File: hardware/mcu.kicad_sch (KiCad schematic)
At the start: 0 parts

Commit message: RP2350B core sheet: MCU, regulator, crystal, QSPI flash, PSRAM, USB-C, buttons, SWD
- scripts/schlib.py: resolve chained (extends) symbols
- gen_mcu.py: GPIO nets per the architecture map; USB-C data only with Rd

Co-Authored-By: Claude Fable 5.1 <noreply@anthropic.com>
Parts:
- added C20, C21, C22: 4.7u, Capacitor_SMD:C_0805_2012Metric, symbol Device:C
- added C23, C24, C25, C26, C27, C28, C29, C30, C31, C32, C33, C34, C37, C38: 100n, Capacitor_SMD:C_0603_1608Metric, symbol Device:C
- added C35, C36: 15p, Capacitor_SMD:C_0603_1608Metric, symbol Device:C
- added J1: USB-C, Connector_USB:USB_C_Receptacle_HRO_TYPE-C-31-M-12, symbol Connector:USB_C_Receptacle_USB2.0_16P
- added L1: 3.3uH, Inductor_SMD:L_1008_2520Metric, symbol Device:L
- added R20, R23: 1k, Resistor_SMD:R_0603_1608Metric, symbol Device:R
- added R21, R22: 10k, Resistor_SMD:R_0603_1608Metric, symbol Device:R
- added R24, R25: 5k1, Resistor_SMD:R_0603_1608Metric, symbol Device:R
- added R26, R27: 27, Resistor_SMD:R_0603_1608Metric, symbol Device:R
- added SW3: RUN, Button_Switch_SMD:SW_SPST_PTS645Sx43SMTR92, symbol Switch:SW_Push
- added SW4: BOOTSEL, Button_Switch_SMD:SW_SPST_PTS645Sx43SMTR92, symbol Switch:SW_Push
- added TP1: SWCLK, TestPoint:TestPoint_Pad_1.5x1.5mm, symbol Connector:TestPoint
- added TP2: SWDIO, TestPoint:TestPoint_Pad_1.5x1.5mm, symbol Connector:TestPoint
- added TP3: GND, TestPoint:TestPoint_Pad_1.5x1.5mm, symbol Connector:TestPoint
- added U20: RP2350B, Package_DFN_QFN:QFN-80-1EP_10x10mm_P0.4mm_EP3.4x3.4mm, symbol MCU_RaspberryPi:RP2350B
- added U21: W25Q128JVSIQ, Package_SO:SOIC-8_5.3x5.3mm_P1.27mm, symbol Memory_Flash:W25Q128JVS
- added U22: APS6404L-3SQR-SN, Package_SO:SOIC-8_5.3x5.3mm_P1.27mm, symbol Memory_RAM:APS6404L-3SQRx-SN
- added Y1: 12MHz, Crystal:Crystal_SMD_3225-4Pin_3.2x2.5mm, symbol Device:Crystal_GND24
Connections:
- new net: J1.A4 (VBUS), J1.A9 (VBUS), J1.B4 (VBUS), J1.B9 (VBUS)
- new net +3V3: C22.1, C23.1, C24.1, C25.1, C26.1, C27.1, C28.1, C29.1, C30.1, C31.1, C32.1, C33.1, C34.1, C37.1, C38.1, R21.1, R22.1, U20.15 (IOVDD), U20.24 (IOVDD), U20.29 (IOVDD), U20.41 (IOVDD), U20.5 (IOVDD), U20.50 (IOVDD), U20.59 (ADC_AVDD), U20.60 (IOVDD), U20.61 (VREG_AVDD), U20.64 (VREG_VIN), U20.68 (USB_OTP_VDD), U20.69 (QSPI_IOVDD), U20.76 (IOVDD), U21.8 (VCC), U22.8 (VDD)
- new net ASEL: U20.6 (GPIO8)
- new net AUDIO_L: U20.57 (GPIO46/ADC6)
- new net AUDIO_R: U20.38 (GPIO30)
- new net BE_REQ: U20.9 (GPIO11)
- new net BOOTSEL_SW: R23.2, SW4.1
- new net CC1: J1.A5 (CC1), R24.1
- new net CC2: J1.B5 (CC2), R25.1
- new net DVDD: C20.1, C21.1, L1.2, U20.10 (DVDD), U20.32 (DVDD), U20.51 (DVDD), U20.65 (VREG_FB)
- new net GND: C20.2, C21.2, C22.2, C23.2, C24.2, C25.2, C26.2, C27.2, C28.2, C29.2, C30.2, C31.2, C32.2, C33.2, C34.2, C35.2, C36.2, C37.2, C38.2, J1.A1 (GND), J1.A12 (GND), J1.B1 (GND), J1.B12 (GND), J1.SH (SHIELD), R24.2, R25.2, SW3.2, SW4.2, TP3.1, U20.62 (VREG_PGND), U20.81 (GND), U21.4 (GND), U22.4 (VSS), Y1.2 (G), Y1.4 (G)
- new net MD0: U20.77 (GPIO0)
- new net MD1: U20.78 (GPIO1)
- new net MD2: U20.79 (GPIO2)
- new net MD3: U20.80 (GPIO3)
- new net MD4: U20.1 (GPIO4)
- new net MD5: U20.2 (GPIO5)
- new net MD6: U20.3 (GPIO6)
- new net MD7: U20.4 (GPIO7)
- new net OLED_CS: U20.52 (GPIO41/ADC1)
- new net OLED_DC: U20.49 (GPIO40/ADC0)
- new net OLED_MOSI: U20.54 (GPIO43/ADC3)
- new net OLED_SCK: U20.53 (GPIO42/ADC2)
- new net PSRAM_CS: U20.58 (GPIO47/ADC7), U22.1 (~{CE})
- new net QSPI_SCLK: U20.71 (QSPI_SCLK), U21.6 (CLK), U22.6 (SCLK)
- new net QSPI_SD0: U20.72 (QSPI_SD0), U21.5 (DI/IO_{0}), U22.5 (SI/SIO0)
- new net QSPI_SD1: U20.74 (QSPI_SD1), U21.2 (DO/IO_{1}), U22.2 (SO/SIO1)
- new net QSPI_SD2: U20.73 (QSPI_SD2), U21.3 (~{WP}/IO_{2}), U22.3 (SIO2)
- new net QSPI_SD3: U20.70 (QSPI_SD3), U21.7 (~{HOLD}/~{RESET}/IO_{3}), U22.7 (SIO3)
- new net REG_SEL0: U20.25 (GPIO24)
- new net REG_SEL1: U20.26 (GPIO25)
- new net RESET_HOLD: U20.37 (GPIO29)
- new net RUN: R22.2, SW3.1, U20.35 (RUN)
- new net SD_CS: U20.46 (GPIO37)
- new net SD_MISO: U20.45 (GPIO36)
- new net SD_MOSI: U20.48 (GPIO39)
- new net SD_SCK: U20.47 (GPIO38)
- new net SWCLK: TP1.1, U20.33 (SWCLK)
- new net SWDIO: TP2.1, U20.34 (SWDIO)
- new net TAPE_IN: U20.22 (GPIO22)
- new net TAPE_OUT: U20.23 (GPIO23)
- new net USB_DM: R27.2, U20.66 (USB_DM)
- new net USB_DM_C: J1.A7 (D-), J1.B7 (D-), R27.1
- new net USB_DP: R26.2, U20.67 (USB_DP)
- new net USB_DP_C: J1.A6 (D+), J1.B6 (D+), R26.1
- new net VREG_LX: L1.1, U20.63 (VREG_LX)
- new net WAIT_REQ: U20.11 (GPIO12)
- new net WIFI_RX: U20.56 (GPIO45/ADC5)
- new net WIFI_TX: U20.55 (GPIO44/ADC4)
- new net XIN: C35.1, U20.30 (XIN), Y1.1
- new net XOUT: R20.1, U20.31 (XOUT)
- new net XOUT_R: C36.1, R20.2, Y1.3
- new net Z80_A14: U20.12 (GPIO13)
- new net Z80_A15: U20.13 (GPIO14)
- new net nAOE: U20.7 (GPIO9)
- new net nDATA_OE: U20.8 (GPIO10)
- new net nEXROM_L: U20.20 (GPIO20)
- new net nINT_L: U20.21 (GPIO21)
- new net nIORQ_V: U20.16 (GPIO16)
- new net nMRD: U20.28 (GPIO27)
- new net nMREQ_V: U20.14 (GPIO15)
- new net nMWR: U20.36 (GPIO28)
- new net nQSPI_SS: R21.2, R23.1, U20.75 (~{QSPI_SS}), U21.1 (~{CS})
- new net nRD_L: U20.17 (GPIO17)
- new net nREG_STB: U20.27 (GPIO26)
- new net nROSCS_L: U20.19 (GPIO19)
- new net nWR_L: U20.18 (GPIO18)
- no-connect marks 0 -> 11
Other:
- note added: "C23-C34: one per IOVDD, QSPI_IOVDD, USB_OTP_VDD, ADC_AVDD, VREG_AVDD pin, placed at the pin."
- note added: "CS1 = GPIO47 (QMI CS1n). C37/C38 at U21/U22."
- note added: "J1: USB 2.0 only. VBUS and SBU unconnected."
- note added: "L1/C20/C21: RP2350 internal 1.1 V core regulator. C22 at VREG_VIN."
- note added: "R24/R25 5.1 k Rd. R26/R27 27 R series."
- note added: "RP2350B core per the RP2350 hardware design guide. GPIO map: docs/v3-architecture.md section 7. GP31-GP35 spare."
- note added: "TP1-TP3: SWD debug pads."
- note added: "U21 boot flash (XIP CS0). U22 PSRAM on the same QSPI bus,"
- note added: "USB-C is data only: VBUS is not connected to the card. Rd on CC1/CC2 so a Type-C host attaches."
- note added: "Y1: 12 MHz, e.g. ABM8-272-T3 (CL 10 pF). C35/C36 15 pF, R20 1 k in series with XOUT."
- note removed: "RP2350B, W25Q128 QSPI flash, APS6404L PSRAM (CS1=GP47), 12 MHz crystal, USB-C, BOOTSEL/RUN, SWD pads"

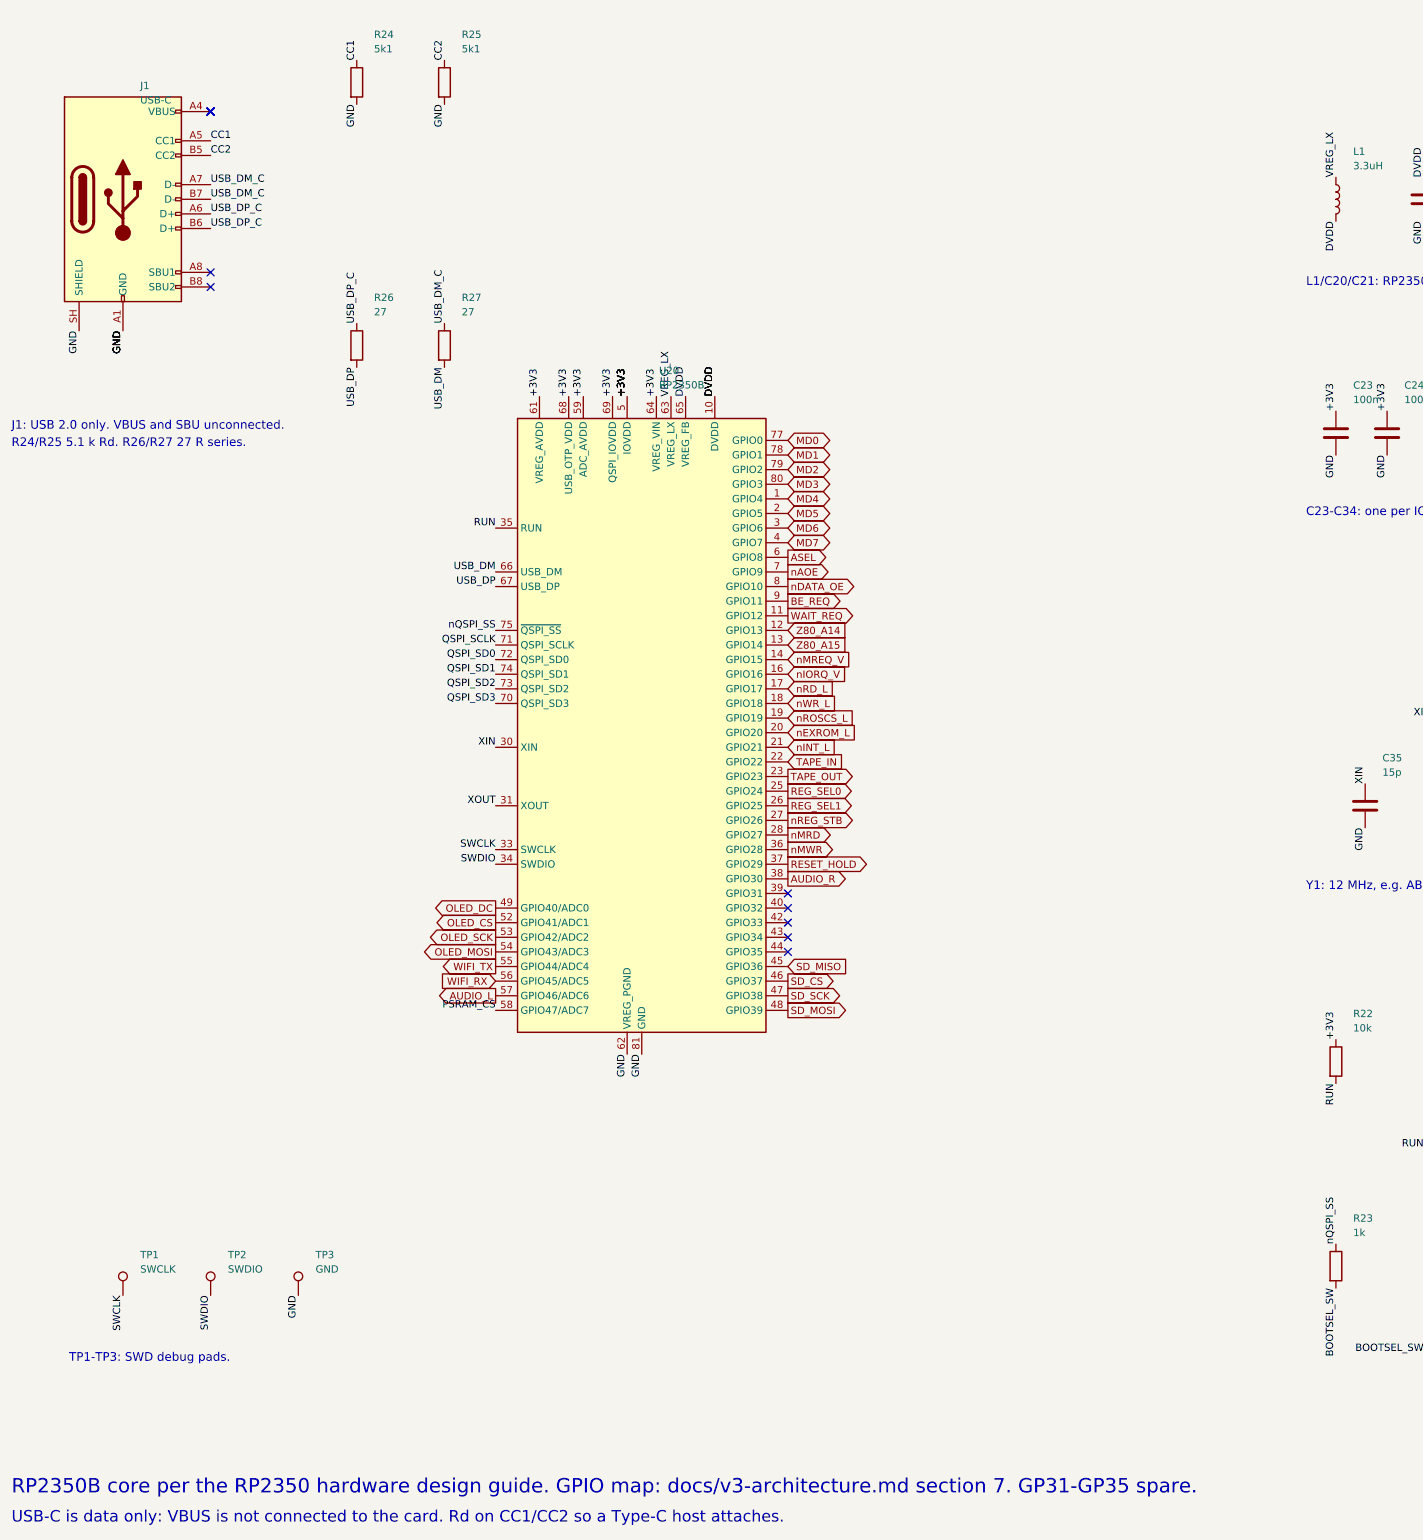
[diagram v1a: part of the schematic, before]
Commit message: Remaining sheets: power, SD and display, WiFi, audio, joystick; ERC clean
- Power: Schottky diode-OR of edge +5V and USB VBUS (card runs from the
  2068/expansion bus, USB alone, or both), two TLV1117LV33 LDOs, bulk caps
- SD: Hirose DM3AT in SPI mode with series R, pull-ups, card detect to STAT
- OLED: 7-pin header (Waveshare 1.27in 128x96 SSD1351) on SPI1
- WiFi: ESP32-C3-WROOM-02 on UART, EN/boot from CTL, IO8 pull-up
- Audio: PWM low-pass, 2068 SOUND mix, MCP6002 buffers, 3.5 mm jack
- Joystick: DE-9 Kempston with pull-ups, series R, optional +5V jumper
- Memory sheet: activity LED on CTL bit 6
- Docs: power decision updated

Co-Authored-By: Claude Fable 5.1 <noreply@anthropic.com>
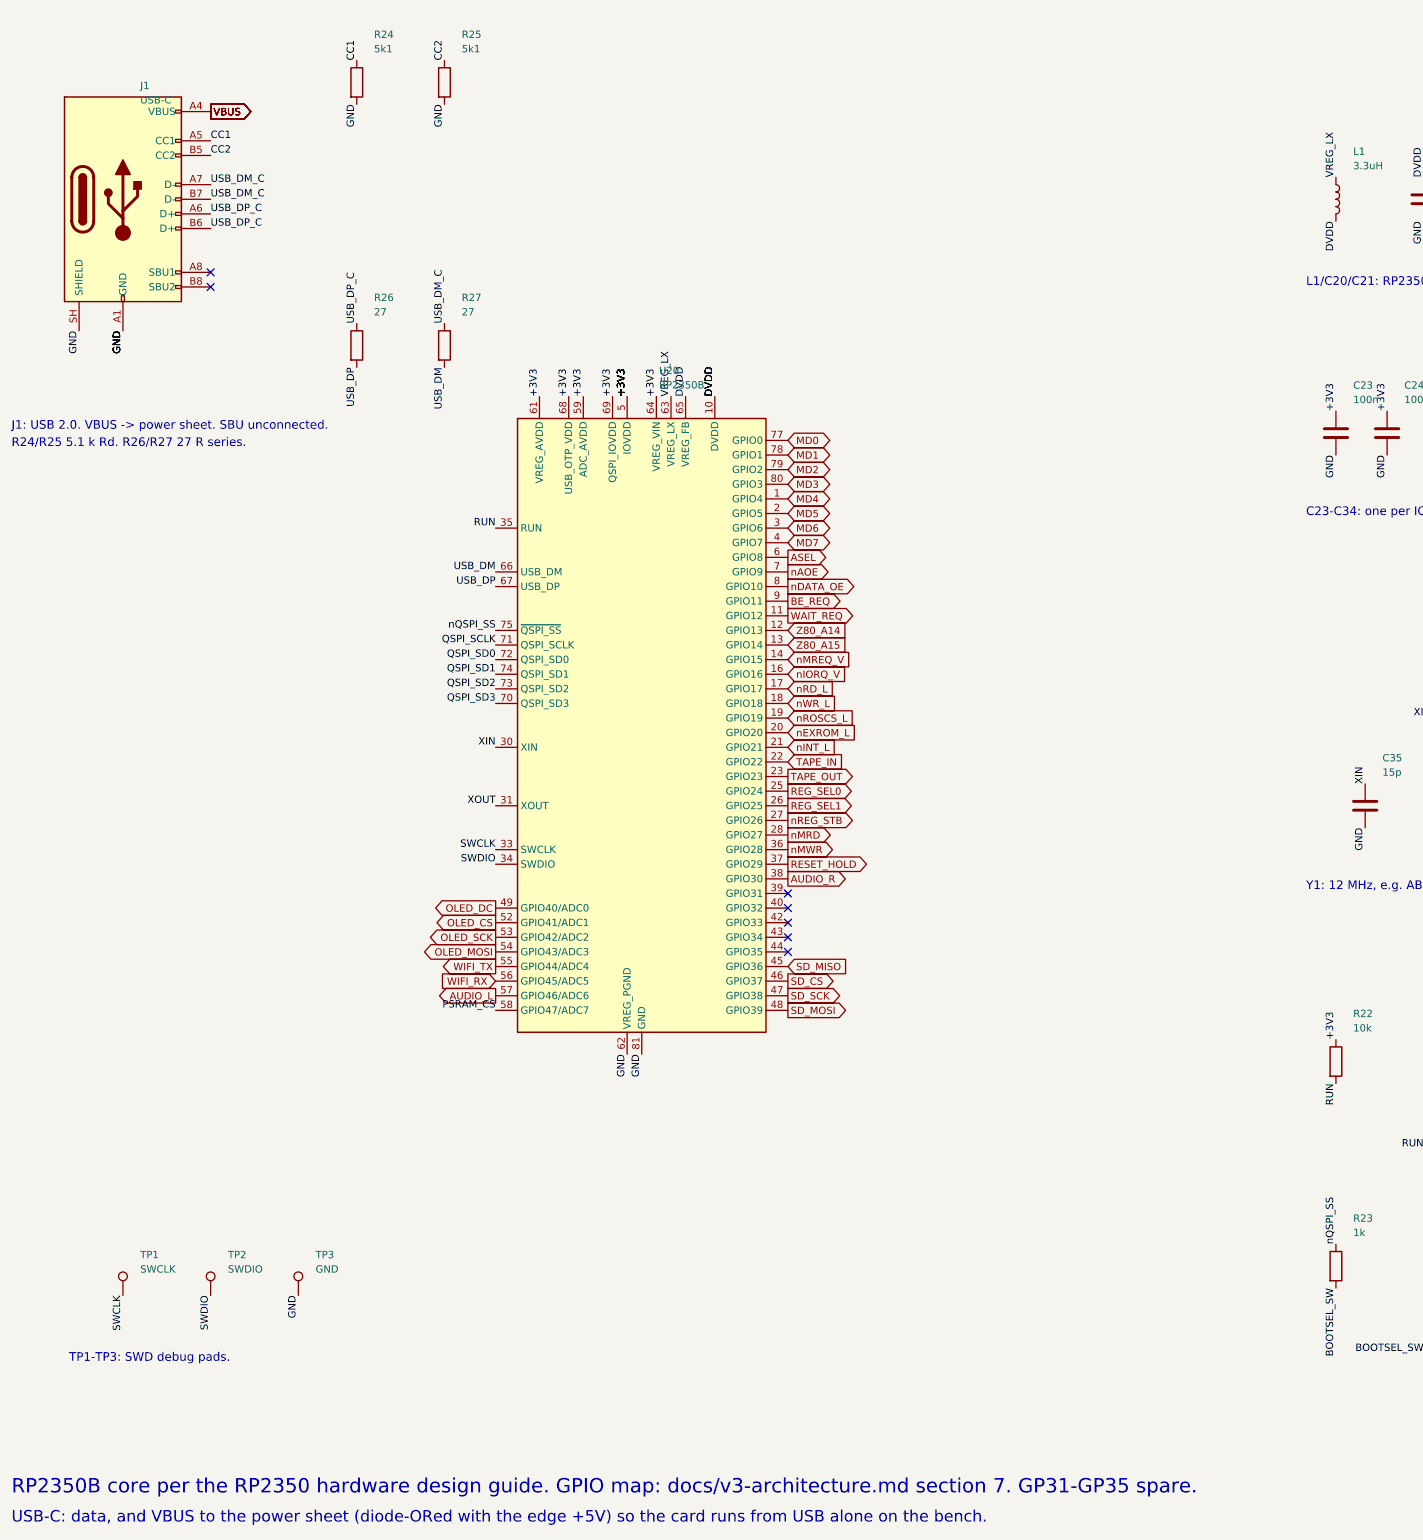
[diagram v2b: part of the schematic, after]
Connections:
- net VBUS: now reaches J1.A4 (VBUS), J1.A9 (VBUS), J1.B4 (VBUS), J1.B9 (VBUS)
- no-connect marks 11 -> 7
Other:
- note added: "J1: USB 2.0. VBUS -> power sheet. SBU unconnected."
- note added: "USB-C: data, and VBUS to the power sheet (diode-ORed with the edge +5V) so the card runs from USB alone on the bench."
- note removed: "J1: USB 2.0 only. VBUS and SBU unconnected."
- note removed: "USB-C is data only: VBUS is not connected to the card. Rd on CC1/CC2 so a Type-C host attaches."
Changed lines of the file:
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@@
   (title_block (title "TS-Pico v3: RP2350B Core") (rev "0.1") (company "Timex/Sinclair Online User Group"))
   (text "RP2350B core per the RP2350 hardware design guide. GPIO map: docs/v3-architecture.md section 7. GP31-GP35 spare." (exclude_from_sim no) (at 20 285 0) (effects (font (size 2.5 2.5)) (justify left bottom)))
-  (text "USB-C is data only: VBUS is not connected to the card. Rd on CC1/CC2 so a Type-C host attaches." (exclude_from_sim no) (at 20 290 0) (effects (font (size 2.0 2.0)) (justify left bottom)))
+  (text "USB-C: data, and VBUS to the power sheet (diode-ORed with the edge +5V) so the card runs from USB alone on the bench." (exclude_from_sim no) (at 20 290 0) (effects (font (size 2.0 2.0)) (justify left bottom)))
   (symbol (lib_id "power:+3V3") (at 299.72 30.48 0) (unit 1)
     (exclude_from_sim no) (in_bom yes) (on_board yes) (dnp no)
@@
     (instances (project "tspico-v3" (path "/9088d141-8624-4d5c-91a9-7a3a7a90b3cc/104b7bea-b03f-4047-9848-946fc1316e79" (reference "J1") (unit 1))))
   )
-  (no_connect (at 54.61 44.45))
-  (no_connect (at 54.61 44.45))
-  (no_connect (at 54.61 44.45))
-  (no_connect (at 54.61 44.45))
+  (global_label "VBUS" (shape output) (at 54.61 44.45 0) (effects (font (size 1.27 1.27)) (justify left)))
+  (global_label "VBUS" (shape output) (at 54.61 44.45 0) (effects (font (size 1.27 1.27)) (justify left)))
+  (global_label "VBUS" (shape output) (at 54.61 44.45 0) (effects (font (size 1.27 1.27)) (justify left)))
+  (global_label "VBUS" (shape output) (at 54.61 44.45 0) (effects (font (size 1.27 1.27)) (justify left)))
   (no_connect (at 54.61 72.39))
   (no_connect (at 54.61 74.93))
@@
   (label "USB_DM_C" (at 95.25 81.28 90) (effects (font (size 1.27 1.27)) (justify left bottom)))
   (label "USB_DM" (at 95.25 88.90 270) (effects (font (size 1.27 1.27)) (justify right bottom)))
-  (text "J1: USB 2.0 only. VBUS and SBU unconnected." (exclude_from_sim no) (at 20 100 0) (effects (font (size 1.5 1.5)) (justify left bottom)))
+  (text "J1: USB 2.0. VBUS -> power sheet. SBU unconnected." (exclude_from_sim no) (at 20 100 0) (effects (font (size 1.5 1.5)) (justify left bottom)))
   (text "R24/R25 5.1 k Rd. R26/R27 27 R series." (exclude_from_sim no) (at 20 103 0) (effects (font (size 1.5 1.5)) (justify left bottom)))
   (symbol (lib_id "Connector:TestPoint") (at 39.37 250.19 0) (unit 1)

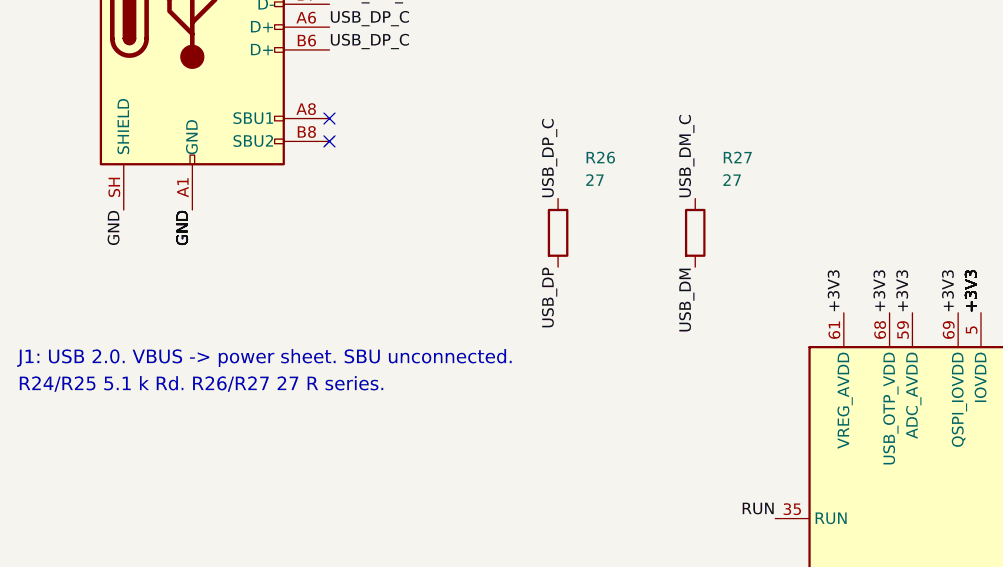
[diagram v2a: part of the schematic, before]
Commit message: BOM pass: LCSC and MPN fields on every part, JLCPCB BOM export
- scripts/parts.py: part table looked up 2026-09-16; schlib stamps fields
- substitutions for stock: 74HC273PW, 74LVC139PW, TI LVC04/08/126/574/1G86,
  33R USB series, XKB TS-1187A switches, Panasonic polymer 220uF, B5819W
- bom/: JLCPCB-format and full BOM CSVs

Co-Authored-By: Claude Fable 5.1 <noreply@anthropic.com>
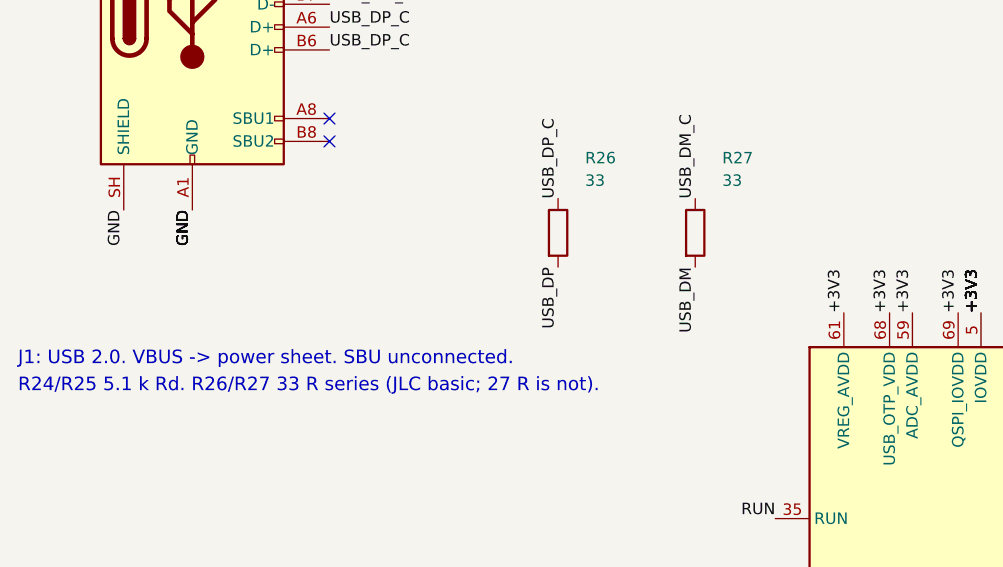
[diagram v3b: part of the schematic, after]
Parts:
- C20, C21, C22: LCSC (none) -> C1779; MPN (none) -> CL21A475KAQNNNE
- C23, C24, C25, C26, C27, C28, C29, C30, C31, C32, C33, C34, C37, C38: LCSC (none) -> C14663; MPN (none) -> CC0603KRX7R9BB104
- C35, C36: LCSC (none) -> C1644; MPN (none) -> CL10C150JB8NNNC
- J1: LCSC (none) -> C165948; MPN (none) -> TYPE-C-31-M-12
- L1: MPN (none) -> SWPA252012S3R3MT
- R20, R23: LCSC (none) -> C21190; MPN (none) -> 0603WAF1001T5E
- R21, R22: LCSC (none) -> C25804; MPN (none) -> 0603WAF1002T5E
- R24, R25: LCSC (none) -> C23186; MPN (none) -> 0603WAF5101T5E
- R26, R27: value 27 -> 33; LCSC (none) -> C23140; MPN (none) -> 0603WAF330JT5E
- SW3, SW4: footprint Button_Switch_SMD:SW_SPST_PTS645Sx43SMTR92 -> Button_Switch_SMD:SW_Push_1P1T_XKB_TS-1187A; LCSC (none) -> C318884; MPN (none) -> TS-1187A-B-A-B
- U20: LCSC (none) -> C42415655; MPN (none) -> RP2350B
- U21: LCSC (none) -> C97521; MPN (none) -> W25Q128JVSIQ
- U22: LCSC (none) -> C5333729; MPN (none) -> APS6404L-3SQR-SN
- Y1: LCSC (none) -> C20625731; MPN (none) -> ABM8-272-T3
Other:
- note added: "R24/R25 5.1 k Rd. R26/R27 33 R series (JLC basic; 27 R is not)."
- note removed: "R24/R25 5.1 k Rd. R26/R27 27 R series."
